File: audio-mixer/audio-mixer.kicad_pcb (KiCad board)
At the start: 2 copper layers, 50 x 100 mm, 9 parts, among them J1 VAL**, J2 10118193-0001LF, J3 RCJ-2234, U1 PDME1-S5-D9-S, U2 LM833M, U3 LM833M, U4 LM833M, U5 LM833M, U6 LM833M

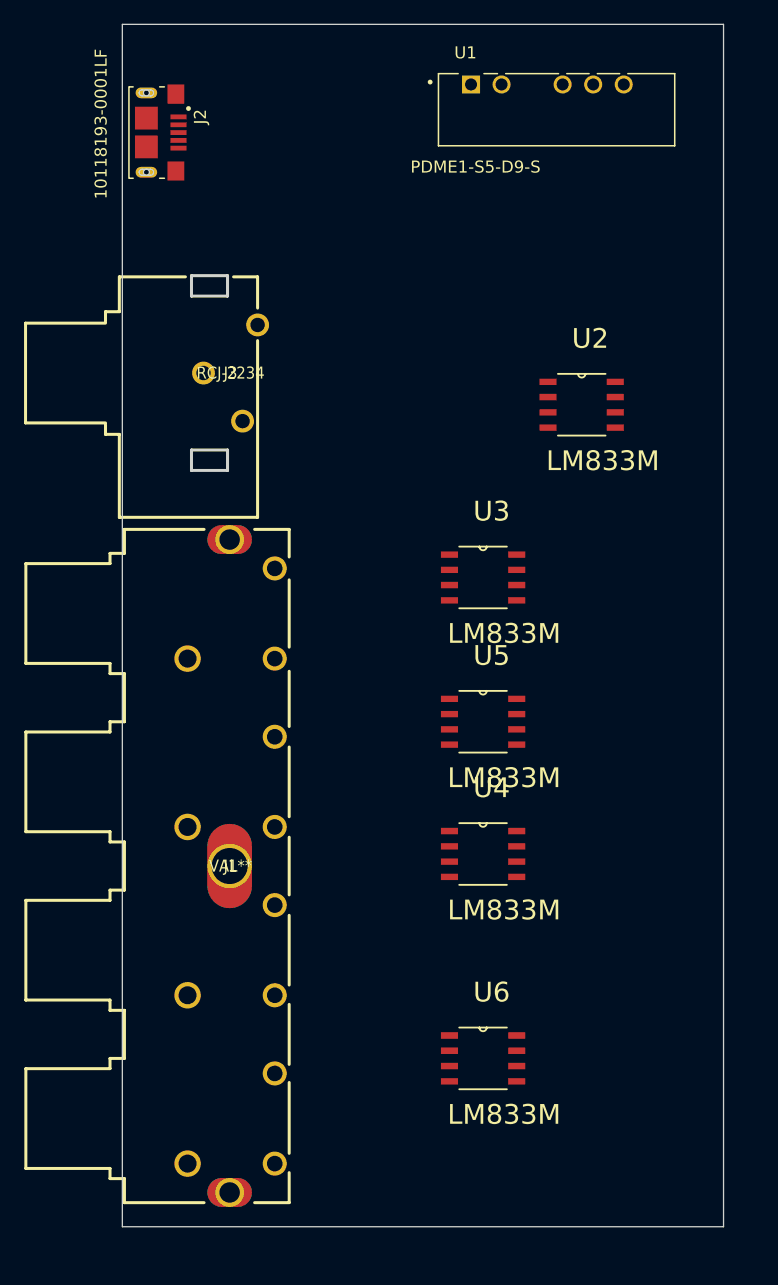
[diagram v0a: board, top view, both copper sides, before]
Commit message: updates schematic
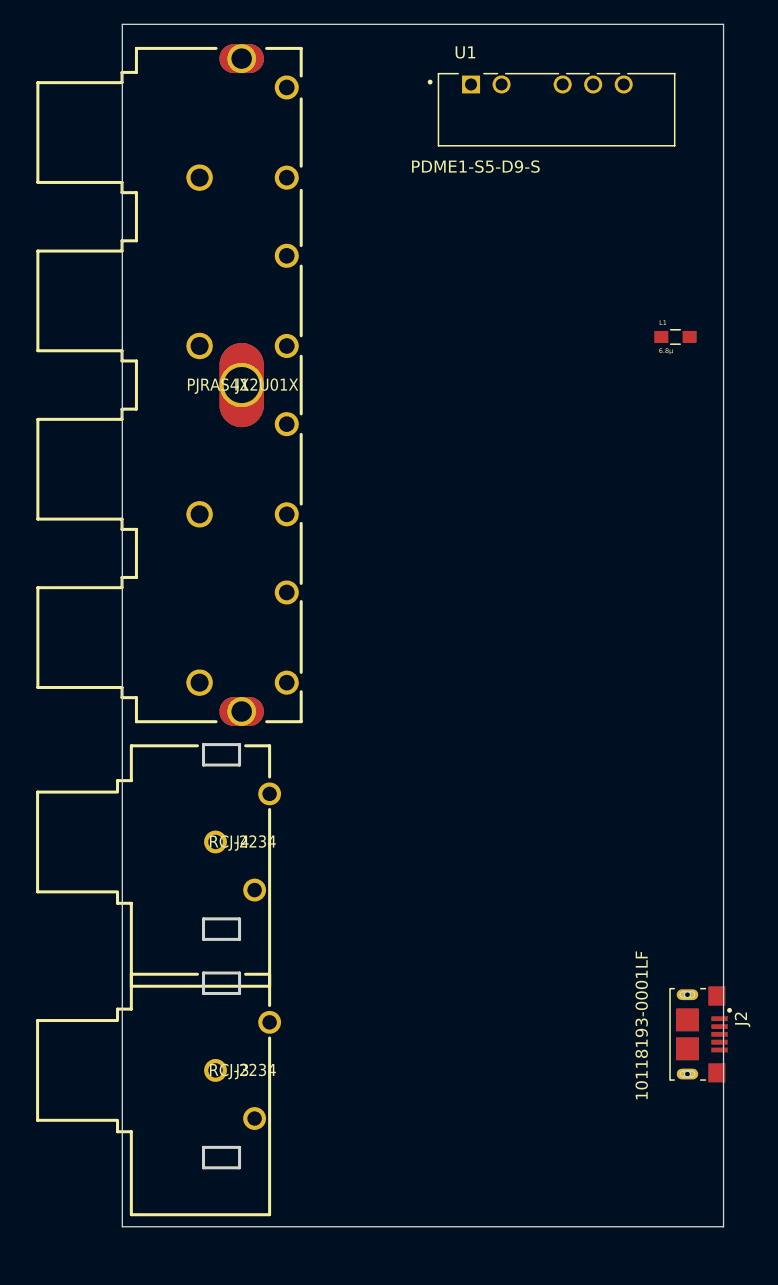
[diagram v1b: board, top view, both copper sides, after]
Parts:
- removed U2, U3, U4, U5, U6: LM833M, LM833M:SOIC127P600X175-8N
- added J4: RCJ-2234, RCJ-2234:RCJ-2221, F.Cu at (93.0, 85.0)
- added L1: 6.8µ, MLZ2012M6R8WT000:INDC2012X87N, F.Cu at (129.0, 43.0)
- J1: value VAL** -> PJRAS4X2U01X
- moved J2 87.5 mm to (130.0, 101.0)
- moved J3 58.0 mm to (93.0, 104.0)
- moved J1 40.0 mm to (93.0, 47.0)
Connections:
- net INPUT1A renamed INPUT1R
- net INPUT1B renamed INPUT1L
- net INPUT2A renamed INPUT2R
- net INPUT2B renamed INPUT2L
- net INPUT3A renamed INPUT3R
- net INPUT3B renamed INPUT3L
- net INPUT4A renamed INPUT4R
- net INPUT4B renamed INPUT4L
- net OUTPUT1A renamed OUTPUT1R
- net OUTPUT1B renamed OUTPUT1L

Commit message: updates pcb
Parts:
- added C10: 1µ, Capacitor_SMD:C_0805_2012Metric, F.Cu at (103.1, 35.0)
- added C11: 50p, Capacitor_SMD:C_0805_2012Metric, F.Cu at (110.8, 64.0)
- added C12: 50p, Capacitor_SMD:C_0805_2012Metric, F.Cu at (115.2, 61.0)
- added C13: 50p, Capacitor_SMD:C_0805_2012Metric, F.Cu at (117.1, 43.0)
- added C14: 50p, Capacitor_SMD:C_0805_2012Metric, F.Cu at (106.4, 69.8)
- added C15: 1µ, Capacitor_SMD:C_0805_2012Metric, F.Cu at (101.1, 58.0)
- added C16: 1µ, Capacitor_SMD:C_0805_2012Metric, F.Cu at (102.1, 50.0)
- added C17: 1µ, Capacitor_SMD:C_0805_2012Metric, F.Cu at (100.1, 69.0)
- added C18: 1µ, Capacitor_SMD:C_0805_2012Metric, F.Cu at (101.1, 61.0)
- added C19: 50p, Capacitor_SMD:C_0805_2012Metric, F.Cu at (106.4, 72.8)
- added C20: 50p, Capacitor_SMD:C_0805_2012Metric, F.Cu at (110.8, 69.8)
- added C21: 50p, Capacitor_SMD:C_0805_2012Metric, F.Cu at (115.2, 66.9)
- added C22: 50p, Capacitor_SMD:C_0805_2012Metric, F.Cu at (119.6, 64.0)
- added C23: 100n, Capacitor_SMD:C_0805_2012Metric, F.Cu at (119.0, 99.0)
- added C24: 100n, Capacitor_SMD:C_0805_2012Metric, F.Cu at (124.0, 61.0)
- added C25: 100n, Capacitor_SMD:C_0805_2012Metric, F.Cu at (110.8, 72.8)
- added C26: 100n, Capacitor_SMD:C_0805_2012Metric, F.Cu at (115.2, 69.8)
- added C3: 1µ, Capacitor_SMD:C_0805_2012Metric, F.Cu at (119.1, 54.0)
- added C4: 1µ, Capacitor_SMD:C_0805_2012Metric, F.Cu at (112.1, 55.0)
- added C5: 100n, Capacitor_SMD:C_0805_2012Metric, F.Cu at (122.1, 48.0)
- added C6: 100n, Capacitor_SMD:C_0805_2012Metric, F.Cu at (127.0, 54.0)
- added C7: 1µ, Capacitor_SMD:C_0805_2012Metric, F.Cu at (103.0, 29.0)
- added C8: 1µ, Capacitor_SMD:C_0805_2012Metric, F.Cu at (105.0, 22.0)
- added C9: 1µ, Capacitor_SMD:C_0805_2012Metric, F.Cu at (102.1, 44.0)
- added R1: 100k, Resistor_SMD:R_0805_2012Metric, F.Cu at (119.6, 66.9)
- added R10: 10k, Resistor_SMD:R_0805_2012Metric, F.Cu at (119.6, 72.8)
- added R11: 10k, Resistor_SMD:R_0805_2012Metric, F.Cu at (124.0, 69.8)
- added R12: 10k, Resistor_SMD:R_0805_2012Metric, F.Cu at (128.5, 66.9)
- added R13: 10k, Resistor_SMD:R_0805_2012Metric, F.Cu at (119.6, 75.8)
- added R14: 10k, Resistor_SMD:R_0805_2012Metric, F.Cu at (124.0, 72.8)
- added R15: 10k, Resistor_SMD:R_0805_2012Metric, F.Cu at (128.5, 69.8)
- added R16: 10k, Resistor_SMD:R_0805_2012Metric, F.Cu at (124.0, 75.8)
- added R2: 100k, Resistor_SMD:R_0805_2012Metric, F.Cu at (124.0, 64.0)
- added R3: 100k, Resistor_SMD:R_0805_2012Metric, F.Cu at (110.8, 75.8)
- added R4: 100k, Resistor_SMD:R_0805_2012Metric, F.Cu at (128.5, 61.0)
- added R5: 100k, Resistor_SMD:R_0805_2012Metric, F.Cu at (115.2, 72.8)
- added R6: 100k, Resistor_SMD:R_0805_2012Metric, F.Cu at (119.6, 69.8)
- added R7: 100k, Resistor_SMD:R_0805_2012Metric, F.Cu at (124.0, 66.9)
- added R8: 100k, Resistor_SMD:R_0805_2012Metric, F.Cu at (128.5, 64.0)
- added R9: 10k, Resistor_SMD:R_0805_2012Metric, F.Cu at (115.2, 75.8)
- J4: value RCJ-2234 -> SJ1-3523N; footprint RCJ-2234:RCJ-2221 -> digikey-footprints:Headphone_Jack_3.5mm_SJ1-3523N
- moved U1 91.1 mm to (126.0, 112.0), turned to 90 degrees
- moved L1 69.7 mm to (119.2, 112.0)
- moved J2 29.5 mm to (104.0, 115.0), turned to 0 degrees
- moved J4 21.5 mm to (85.0, 105.0), turned to 180 degrees
- moved J3 19.0 mm to (93.0, 85.0)
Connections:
- J4 pad 1: Net-(J4-Pad1) -> GND
- J4 pad 2: OUTPUT2L -> OUTPUT2R
- J4 pad 3: OUTPUT2R -> OUTPUT2L

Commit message: updates circuit
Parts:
- added C1: 4.7µ, parts:UWJ1E4R7MCL1GB, F.Cu at (104.0, 107.0)
- added C2: 4.7µ, parts:UWJ1E4R7MCL1GB, F.Cu at (117.0, 112.2)
- added U2: MC33174, Package_SO:SOIC-14_3.9x8.7mm_P1.27mm, F.Cu at (125.0, 37.0)
- added U3: MC33174, Package_SO:SOIC-14_3.9x8.7mm_P1.27mm, F.Cu at (115.0, 33.0)
- added U4: MC33174, Package_SO:SOIC-14_3.9x8.7mm_P1.27mm, F.Cu at (106.0, 94.0)
- C10, C15, C16, C17, C18, C7, C8, C9: footprint Capacitor_SMD:C_0805_2012Metric -> parts:UWJ1E4R7MCL1GB
- moved L1 7.24 mm to (112.0, 111.0)

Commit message: updates pcb
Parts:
- moved C23 51.1 mm to (122.0, 48.0)
- moved C13 41.8 mm to (109.0, 84.0)
- moved U2 40.1 mm to (122.0, 77.0)
- moved C25 37.0 mm to (128.0, 40.0)
- moved R7 35.4 mm to (130.0, 32.0)
- moved C21 34.2 mm to (130.0, 36.0)
- moved U3 29.2 mm to (126.0, 60.0)
- moved R8 28.7 mm to (122.0, 36.0)
- moved C26 24.8 mm to (127.0, 48.0)
- moved C22 24.1 mm to (122.0, 40.0)
- moved R16 22.8 mm to (122.0, 53.0)
- moved C14 19.1 mm to (117.0, 54.0)
- moved R2 17.6 mm to (109.0, 73.0)
- moved C12 17.6 mm to (108.0, 77.0)
- moved R5 17.2 mm to (114.0, 90.0)
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
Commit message: updates pcb
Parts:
- added RV1: 10k LOG, parts:EVJYK6, B.Cu at (110.0, 26.0)
- added RV2: 10k LOG, parts:EVJYK6, B.Cu at (110.0, 42.0)
- added RV3: 10k LOG, parts:EVJYK6, B.Cu at (110.0, 58.0)
- added RV4: 10k LOG, parts:EVJYK6, B.Cu at (110.0, 74.0)
- added RV5: 10k LOG, parts:EVJYK6, B.Cu at (110.0, 106.0)
- added RV6: 10k LOG, parts:EVJYK6, B.Cu at (110.0, 90.0)
- moved C12 54.2 mm to (113.0, 23.0), turned to 180 degrees
- moved U2 51.7 mm to (126.2, 25.5), turned to 270 degrees
- moved C4 50.0 mm to (129.1, 94.0), turned to 180 degrees
- moved R2 48.2 mm to (112.9, 25.0), turned to 180 degrees
- moved R7 48.1 mm to (112.9, 77.0), turned to 180 degrees
- moved C3 47.4 mm to (129.0, 91.0)
- moved C26 46.9 mm to (100.9, 87.0)
- moved R16 46.6 mm to (109.9, 98.0)
- moved C11 46.0 mm to (113.1, 29.0), turned to 180 degrees
- moved R15 43.0 mm to (119.0, 105.0)
- moved C21 42.5 mm to (113.1, 75.0), turned to 180 degrees
- moved R3 42.2 mm to (113.1, 47.0), turned to 180 degrees
- moved R1 40.0 mm to (112.9, 31.0), turned to 180 degrees
- moved C23 39.5 mm to (101.9, 82.0)
- moved C13 39.2 mm to (113.1, 45.0), turned to 180 degrees
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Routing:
- net +12V: track 0.00 -> 100.9 mm
- net Net-(C13-Pad1): track 0.00 -> 30.6 mm
- net Net-(C14-Pad1): track 0.00 -> 28.1 mm
- net Net-(C11-Pad1): track 0.00 -> 19.2 mm
- net Net-(C19-Pad1): track 0.00 -> 18.8 mm
- net Net-(C12-Pad1): track 0.00 -> 14.5 mm
- net Net-(C20-Pad1): track 0.00 -> 14.0 mm
- net Net-(C16-Pad1): track 0.00 -> 11.4 mm
- net Net-(C18-Pad1): track 0.00 -> 11.4 mm
- net Net-(C17-Pad1): track 0.00 -> 11.3 mm
- net Net-(C10-Pad1): track 0.00 -> 9.74 mm
- net Net-(C8-Pad1): track 0.00 -> 7.89 mm
- net Net-(C15-Pad1): track 0.00 -> 7.48 mm
- net GND: track 0.00 -> 6.31 mm
- net Net-(C9-Pad1): track 0.00 -> 6.03 mm
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
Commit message: update circuit
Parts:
- moved R14 65.6 mm to (126.5, 40.6), turned to 90 degrees
- moved R13 61.3 mm to (124.5, 40.6), turned to 90 degrees
- moved R10 58.6 mm to (119.5, 40.4), turned to 90 degrees
- moved R9 51.1 mm to (121.5, 40.4), turned to 90 degrees
- moved R15 32.6 mm to (122.0, 72.5), turned to 90 degrees
- moved R16 27.4 mm to (120.0, 72.5), turned to 90 degrees
- moved R12 24.9 mm to (124.5, 72.4), turned to 90 degrees
- moved R11 19.2 mm to (126.5, 72.4), turned to 90 degrees
- moved C5 15.2 mm to (126.0, 51.9), turned to 90 degrees
- moved C3 4.61 mm to (130.0, 86.5), turned to 90 degrees
- moved C6 3.73 mm to (126.4, 31.4), turned to 270 degrees
- moved C23 3.59 mm to (101.5, 85.6), turned to 90 degrees
- moved C4 3.56 mm to (130.0, 90.6), turned to 90 degrees
- moved C26 3.00 mm to (103.5, 85.4), turned to 90 degrees
- moved C24 2.06 mm to (126.0, 64.0), turned to 270 degrees
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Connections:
- RV3 pad 7: (no net) -> GND
- RV4 pad 7: (no net) -> GND
- RV4 pad 8: (no net) -> GND
- RV5 pad 7: (no net) -> GND
- RV5 pad 8: (no net) -> GND
- RV6 pad 7: (no net) -> GND
- RV6 pad 8: (no net) -> GND
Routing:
- net -12V: track 0.00 -> 103.5 mm, vias 0 -> 2
- net MIXEDL: track 0.00 -> 86.3 mm, vias 0 -> 4
- net MIXEDR: track 0.00 -> 83.7 mm, vias 0 -> 2
- net Net-(C21-Pad1): track 0.00 -> 30.6 mm
- net OUTPUT2R: track 0.00 -> 30.3 mm, vias 0 -> 2
- net OUTPUT1R: track 0.00 -> 29.1 mm, vias 0 -> 2
- net Net-(C22-Pad1): track 0.00 -> 28.3 mm
- net OUTPUT2L: track 0.00 -> 25.1 mm
- net PROC1R: track 0.00 -> 24.6 mm, vias 0 -> 2
- net Net-(C2-Pad1): track 0.00 -> 23.9 mm
- net PROC1L: track 0.00 -> 23.7 mm, vias 0 -> 2
- net VCC: track 0.00 -> 23.4 mm, vias 0 -> 2
- net PROC4R: track 0.00 -> 22.7 mm, vias 0 -> 2
- net PROC2R: track 0.00 -> 21.7 mm, vias 0 -> 2
- net PROC3R: track 0.00 -> 20.8 mm, vias 0 -> 2
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
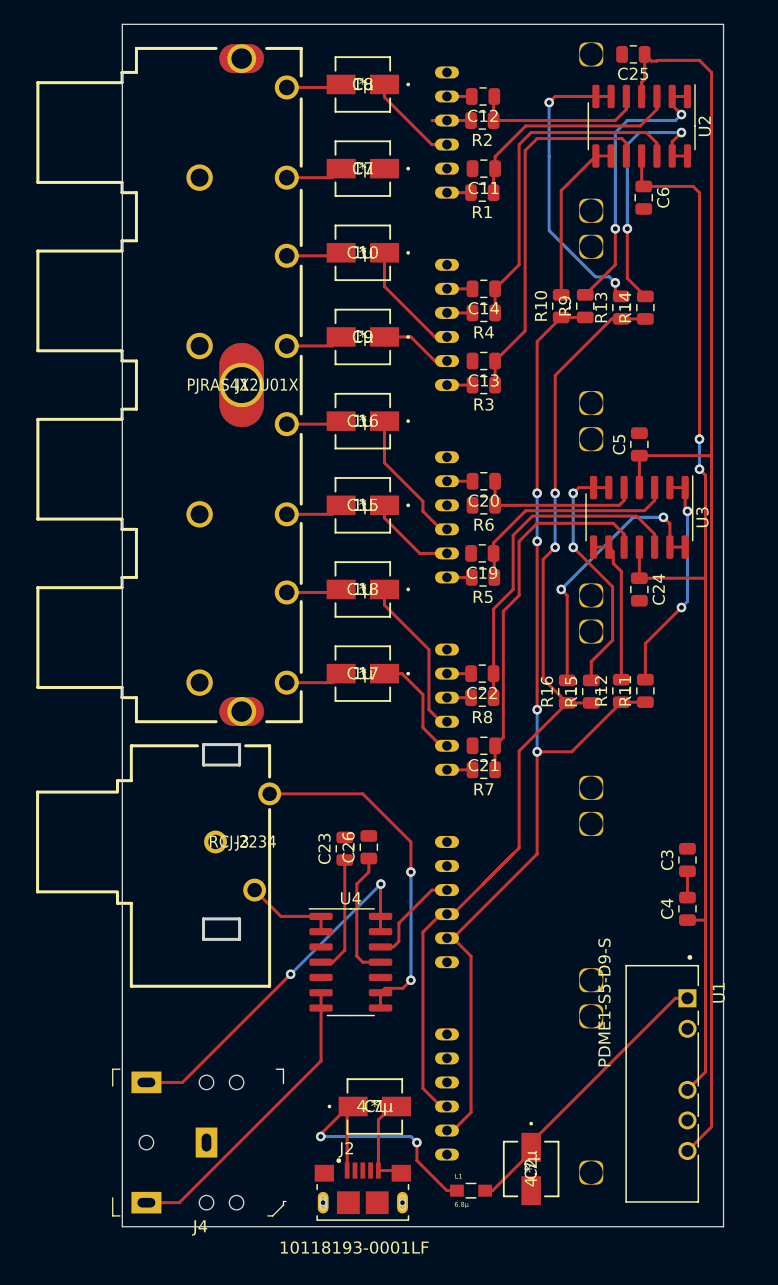
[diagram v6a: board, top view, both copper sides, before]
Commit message: updates pcb and schematic
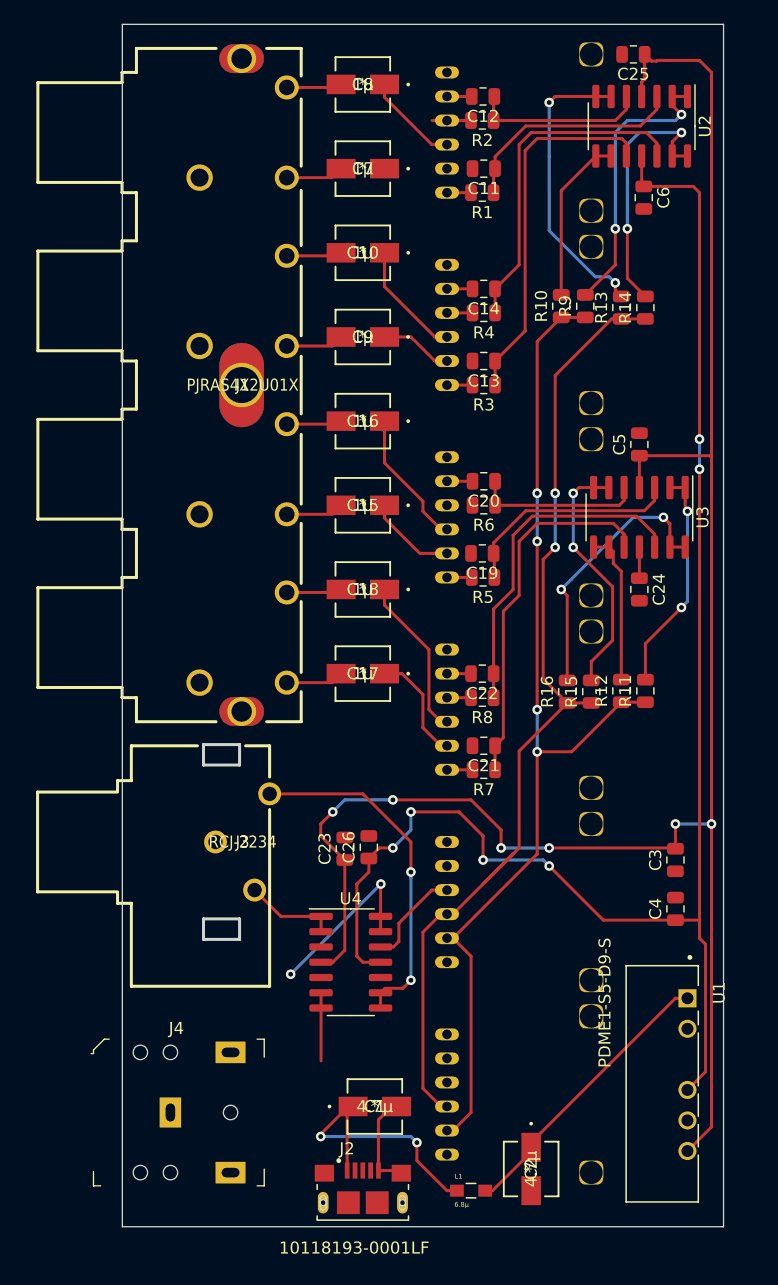
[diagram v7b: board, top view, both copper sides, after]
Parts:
- moved J4 7.43 mm to (92.0, 107.5), turned to 0 degrees
- moved C3 1.00 mm to (129.0, 86.5)
- moved C4 1.00 mm to (129.0, 90.6)
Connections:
- RV1 pad 7: (no net) -> GND
- RV1 pad 8: (no net) -> GND
- RV2 pad 7: (no net) -> GND
- RV2 pad 8: (no net) -> GND
- RV3 pad 8: (no net) -> GND
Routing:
- net +12V: track 119.5 -> 162.3 mm, vias 0 -> 6
- net -12V: track 103.5 -> 131.4 mm, vias 2 -> 6
- net OUTPUT2L: track 25.1 -> 5.67 mm
- net OUTPUT2R: track 30.3 -> 14.6 mm
- net GND: track 18.7 -> 16.5 mm

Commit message: updates pcb
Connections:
- J4 pad 2: OUTPUT2R -> OUTPUT2L
- J4 pad 3: OUTPUT2L -> OUTPUT2R
- RV1 pad 7: GND -> (no net)
- RV1 pad 8: GND -> (no net)
- RV2 pad 7: GND -> (no net)
- RV2 pad 8: GND -> (no net)
- RV3 pad 7: GND -> (no net)
- RV3 pad 8: GND -> (no net)
- RV4 pad 7: GND -> (no net)
- RV4 pad 8: GND -> (no net)
- RV5 pad 7: GND -> (no net)
- RV5 pad 8: GND -> (no net)
- RV6 pad 7: GND -> (no net)
- RV6 pad 8: GND -> (no net)
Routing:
- net Net-(RV5-Pad2): track 0.00 -> 38.8 mm, vias 0 -> 6
- net Net-(RV6-Pad2): track 0.00 -> 32.2 mm, vias 0 -> 6
- net Net-(RV5-Pad5): track 0.00 -> 27.8 mm, vias 0 -> 2
- net OUTPUT2R: track 14.6 -> 36.1 mm
- net OUTPUT2L: track 5.67 -> 21.5 mm
- net Net-(R6-Pad2): track 0.50 -> 2.62 mm
- net MIXEDL: track 86.3 -> 88.0 mm
